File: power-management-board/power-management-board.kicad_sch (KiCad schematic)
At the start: 51 parts, among them IC1 LM74502QDDFRQ1, IC2 TLP7820_TP4,E, J1 Conn_01x02, J2 Conn_01x02, J3 Conn_01x03, J4 Conn_01x04, Q1 XPQR8308QB,LXHQ, Q2 XPQR8308QB,LXHQ, U1 TLP293, U2 TLP293, U3 TLP293, U4 TLP293, U5 TLP3546A, U6 CZ3A07, U7 AP7375

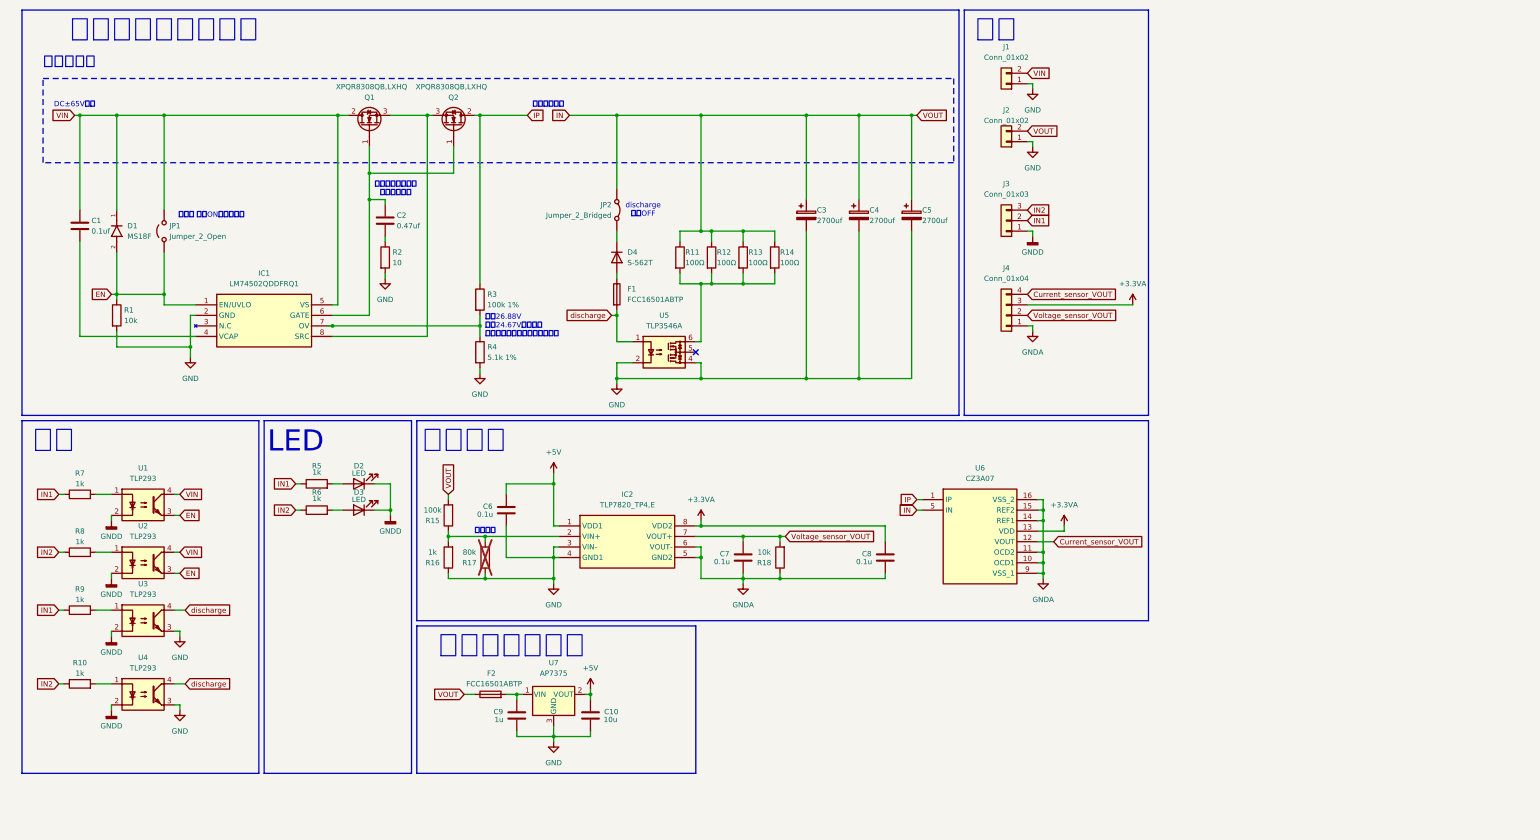
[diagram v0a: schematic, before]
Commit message: 修正版(非常停止はあとで変更します)
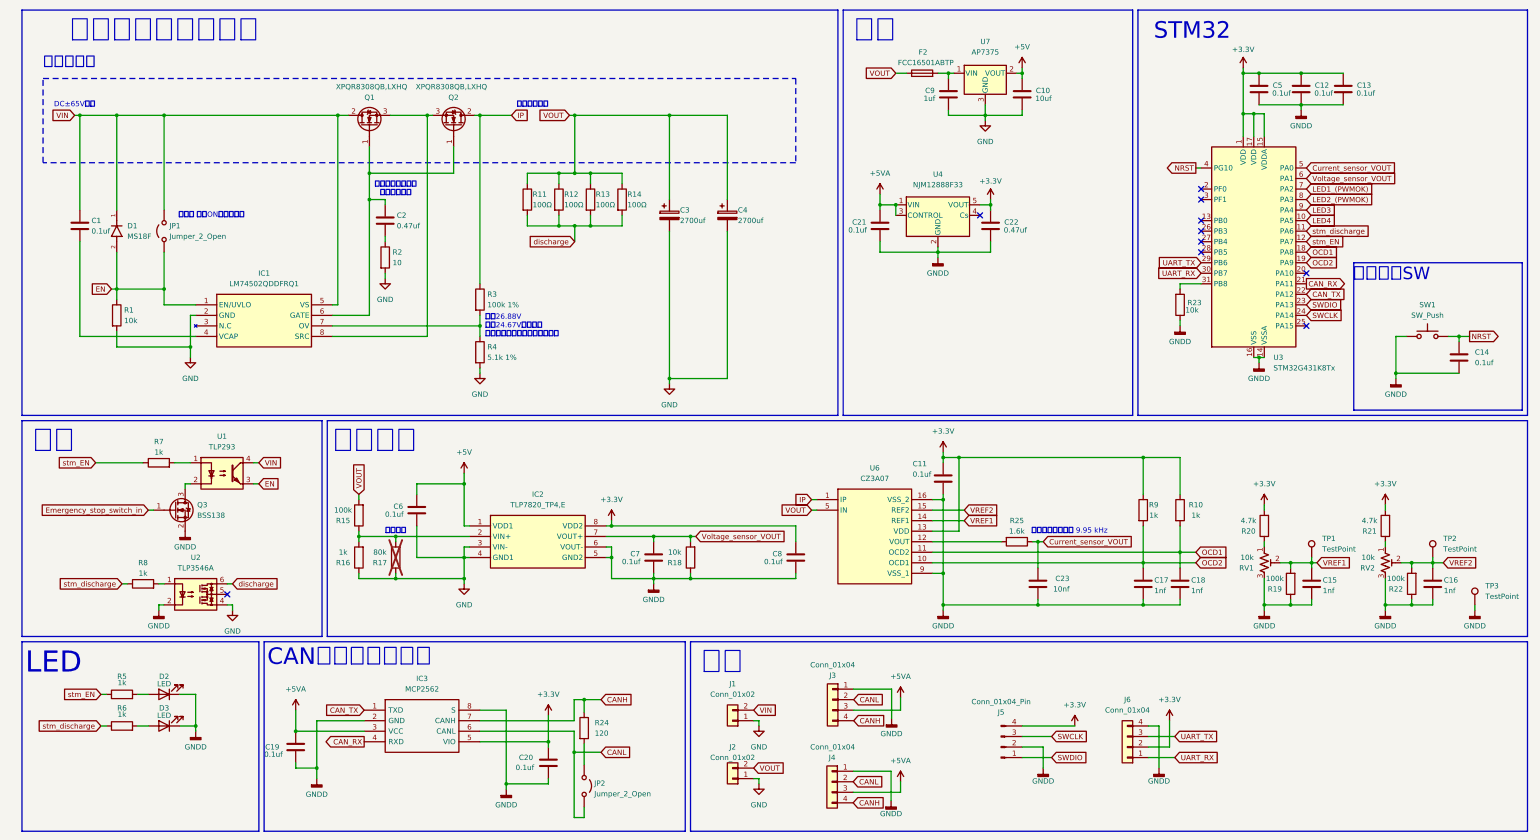
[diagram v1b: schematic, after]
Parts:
- removed C5: 2700uf, Capacitor_THT:CP_Radial_D18.0mm_P7.50mm, symbol Device:C_Polarized
- removed D4: S-562T, 0Ikedalibrary:S-562T, symbol Device:D
- removed F1: FCC16501ABTP, Fuse:Fuse_0603_1608Metric_Pad1.05x0.95mm_HandSolder, symbol Device:Fuse
- removed J3: Conn_01x03, Connector_AMASS:AMASS_MR30PW-M_1x03_P3.50mm_Horizontal, symbol Connector_Generic:Conn_01x03
- removed JP2: Jumper_2_Bridged, Connector_PinHeader_2.54mm:PinHeader_1x02_P2.54mm_Vertical, symbol Jumper:Jumper_2_Bridged
- removed U2, U3, U4: TLP293, Package_SO:SOIC-4_4.55x2.6mm_P1.27mm, symbol Isolator:TLP293
- added C11, C12, C13, C14, C19, C20, C21, C5: 0.1uf, Capacitor_SMD:C_0603_1608Metric_Pad1.08x0.95mm_HandSolder, symbol Device:C
- added C15, C16, C17, C18: 1nf, Capacitor_SMD:C_0603_1608Metric_Pad1.08x0.95mm_HandSolder, symbol Device:C
- added C22: 0.47uf, Capacitor_SMD:C_0603_1608Metric_Pad1.08x0.95mm_HandSolder, symbol Device:C
- added C23: 10nf, Capacitor_SMD:C_0603_1608Metric_Pad1.08x0.95mm_HandSolder, symbol Device:C
- added IC3: MCP2562, 0Ikedalibrary:SOIC127P600X175-8N, symbol 0-Myparts:TJA1441AT_0Z
- added J3, J6: Conn_01x04, Connector_JST:JST_XH_S4B-XH-A_1x04_P2.50mm_Horizontal, symbol Connector_Generic:Conn_01x04
- added J5: Conn_01x04_Pin, Connector_PinHeader_2.54mm:PinHeader_1x04_P2.54mm_Vertical, symbol Connector:Conn_01x04_Pin
- added JP2: Jumper_2_Open, TestPoint:TestPoint_2Pads_Pitch2.54mm_Drill0.8mm, symbol Jumper:Jumper_2_Open
- added Q3: BSS138, Package_TO_SOT_SMD:SOT-23, symbol Transistor_FET:BSS138
- added R19, R22: 100k, Resistor_SMD:R_0603_1608Metric_Pad0.98x0.95mm_HandSolder, symbol Device:R
- added R20, R21: 4.7k, Resistor_SMD:R_0603_1608Metric_Pad0.98x0.95mm_HandSolder, symbol Device:R
- added R23: 10k, Resistor_SMD:R_0603_1608Metric_Pad0.98x0.95mm_HandSolder, symbol Device:R
- added R24: 120, Resistor_SMD:R_0603_1608Metric_Pad0.98x0.95mm_HandSolder, symbol Device:R
- added R25: 1.6k, Resistor_SMD:R_0603_1608Metric_Pad0.98x0.95mm_HandSolder, symbol Device:R
- added RV1, RV2: 10k, Connector_PinHeader_2.54mm:PinHeader_1x03_P2.54mm_Vertical, symbol Device:R_Potentiometer_Trim_US
- added SW1: SW_Push, 0Ikedalibrary:switch_TVAF06-A020B-R, symbol Switch:SW_Push
- added TP1, TP2, TP3: TestPoint, TestPoint:TestPoint_Loop_D1.80mm_Drill1.0mm_Beaded, symbol Connector:TestPoint
- added U3: STM32G431K8Tx, Package_QFP:LQFP-32_7x7mm_P0.8mm, symbol MCU_ST_STM32G4:STM32G431K8Tx
- added U4: NJM12888F33, Package_TO_SOT_SMD:SOT-23-5_HandSoldering, symbol Regulator_Linear:LDK130PU33R_DFN6
- C10: value 10u -> 10uf
- C6, C7, C8: value 0.1u -> 0.1uf
- C9: value 1u -> 1uf
- IC1: footprint SOT65P280X110-8N -> Package_TO_SOT_SMD:SOT-23-8_Handsoldering
- J4: footprint Connector_JST:JST_XH_B4B-XH-A_1x04_P2.50mm_Vertical -> Connector_JST:JST_XH_S4B-XH-A_1x04_P2.50mm_Horizontal
- renumbered U5 to U2
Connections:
- net Current_sensor_VOUT: now also C23.2, R25.1, U3.5 (PA0); no longer J4.4 (Pin_4), U6.12 (VOUT)
- net GND: no longer U2.2
- net GNDD: now also C7.2, C8.2, IC2.5 (GND2), IC2.6 (VOUT-), J4.1 (Pin_1), R18.1, U2.2, U6.16 (VSS_2), U6.9 (VSS_1), C11.2, C12.2, C13.2, C14.2, C15.2, C16.2, C17.2, C18.2, C19.2, C20.2, C21.2, C22.2, C23.1, C5.2, IC3.2 (GND), IC3.8 (S), J3.1 (Pin_1), J5.2 (Pin_2), J6.4 (Pin_4), Q3.2 (S), R19.1, R22.1, R23.1, RV1.3, RV2.3, SW1.1, TP3.1, U3.14 (VSSA), U3.16 (VSS), U3.32 (VSS), U4.2 (GND); no longer U1.2
- net Voltage_sensor_VOUT: now also U3.6 (PA1); no longer J4.2 (Pin_2)
- net discharge: now also R11.2, R12.2, R13.2, R14.2, U2.6; no longer U2.1
- net OCD2: now reaches R9.2
- net OCD2: now also U6.10 (OCD1), C17.1, U3.19 (PA9)
- net at R8.2: now also U2.1
- net OCD1: now reaches R10.2
- net OCD1: now also U6.11 (OCD2), C18.1, U3.18 (PA8)
- net +3.3VA renamed +3.3V
- net +3.3V: now also R10.1, R9.1, C11.1, C12.1, C13.1, C20.1, C22.1, C5.1, IC3.5 (VIO), J5.4 (Pin_4), J6.2 (Pin_2), R20.2, R21.2, U3.1 (VDD), U3.15 (VDDA), U3.17 (VDD), U4.5 (VOUT); no longer J4.3 (Pin_3)
- removed net GNDA: C7.2, C8.2, IC2.5 (GND2), IC2.6 (VOUT-), J4.1 (Pin_1), R18.1, U6.10 (OCD1), U6.11 (OCD2), U6.14 (REF1), U6.15 (REF2), U6.16 (VSS_2), U6.9 (VSS_1)
- net IN renamed VOUT
- net IN1 renamed stm_EN
- net stm_EN: now also U3.12 (PA7); no longer R9.1
- net IN2 renamed stm_discharge
- net stm_discharge: now also U3.11 (PA6); no longer R10.1
- new net: Q3.3 (D), U1.2
- new net: R20.1, RV1.1
- new net: R23.2, U3.31 (PB8)
- new net: R21.1, RV2.1
- new net: JP2.1 (A), R24.2
- new net: R25.2, U6.12 (VOUT)
- new net +5VA: C19.1, C21.1, IC3.3 (VCC), J3.3 (Pin_3), J4.3 (Pin_3), U4.1 (VIN), U4.3 (CONTROL)
- new net CANH: IC3.7 (CANH), J3.4 (Pin_4), J4.4 (Pin_4), R24.1
- new net CANL: IC3.6 (CANL), J3.2 (Pin_2), J4.2 (Pin_2), JP2.2 (B)
- new net CAN_RX: IC3.4 (RXD), U3.21 (PA11)
- new net CAN_TX: IC3.1 (TXD), U3.22 (PA12)
- new net Emergency_stop_switch_in: Q3.1 (G)
- new net LED1_(PWMOK): U3.7 (PA2)
- new net LED2_(PWMOK): U3.8 (PA3)
- new net LED3: U3.9 (PA4)
- new net LED4: U3.10 (PA5)
- new net NRST: C14.1, SW1.2, U3.4 (PG10)
- new net SWCLK: J5.3 (Pin_3), U3.24 (PA14)
- new net SWDIO: J5.1 (Pin_1), U3.23 (PA13)
- new net UART_RX: J6.1 (Pin_1), U3.30 (PB7)
- new net UART_TX: J6.3 (Pin_3), U3.29 (PB6)
- new net VREF1: C15.1, R19.2, RV1.2, TP1.1, U6.14 (REF1)
- new net VREF2: C16.1, R22.2, RV2.2, TP2.1, U6.15 (REF2)
- no-connect marks 1 -> 10
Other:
- note added: "CANトランシーバー"
- note added: "STM32"
- note added: "リセットSW"
- note added: "ローパスフィルタ 9.95 kHz"
- note added: "電源"
- note removed: "discharge 常時OFF"
- note removed: "センサー用電源"
- moved on the sheet: C10, C3, C4, C6, C7, C8, C9, D2, D3, F2, IC2, J1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

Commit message: 修正版完成
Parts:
- removed Q3: BSS138, Package_TO_SOT_SMD:SOT-23, symbol Transistor_FET:BSS138
- added D4, D8: SS2040FL, 0Ikedalibrary:SOD-123FL, symbol Device:D
- added D5, D6, D7: LED, LED_SMD:LED_0603_1608Metric_Pad1.05x0.95mm_HandSolder, symbol Device:LED
- added J7, J8: Conn_01x02, 0Ikedalibrary:AMASS_XT60-F_1x02_P7.20mm_Vertical, symbol Connector_Generic:Conn_01x02
- added R26: 10k, Resistor_SMD:R_0603_1608Metric_Pad0.98x0.95mm_HandSolder, symbol Device:R
- added R27, R28, R29: 1k, Resistor_SMD:R_0603_1608Metric_Pad0.98x0.95mm_HandSolder, symbol Device:R
- added R30: 100, Resistor_SMD:R_0603_1608Metric_Pad0.98x0.95mm_HandSolder, symbol Device:R
- added U5: TLP293, Package_SO:SOIC-4_4.55x2.6mm_P1.27mm, symbol Isolator:TLP293
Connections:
- net +3.3V: now also R29.1
- net Emergency_stop_switch_in: now also R7.1, J8.2 (Pin_2), R27.1, R28.1
- net GNDD: now also D8.2 (A), J7.1 (Pin_1), R26.2, U5.3
- net stm_EN: no longer R7.1, U3.12 (PA7)
- net GNDA: now reaches U1.2
- net GNDA: now also D5.2 (A), D6.1 (K), D7.2 (A), J8.1 (Pin_1), U5.2
- net at R7.2, U1.1: now also D5.1 (K)
- net EN_return: now reaches U3.20 (PA10)
- net EN_return: now also R29.2, U5.4
- new net: D7.1 (K), R28.2, U5.1
- new net: J7.2 (Pin_2), R30.1
- new net: D6.2 (A), R27.2
- new net Emergency_stop_switch_out: D4.1 (K), D8.1 (K), R30.2
- new net stm32_EN: D4.2 (A), R26.1, U3.12 (PA7)
- no-connect marks 10 -> 9
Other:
- moved on the sheet: C11, C14, C15, C16, C17, C18, C19, C20, C23, C6, C7, C8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

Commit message: 仮配置完了
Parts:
- removed D5, D7: LED, LED_SMD:LED_0603_1608Metric_Pad1.05x0.95mm_HandSolder, symbol Device:LED
- removed J6: Conn_01x04, Connector_JST:JST_XH_S4B-XH-A_1x04_P2.50mm_Horizontal, symbol Connector_Generic:Conn_01x04
- added D10, D5, D7, D9: SS2040FL, 0Ikedalibrary:SOD-123FL, symbol Device:D
- added D11, D12, D13, D14, D15, D16, D17, D18: LED, LED_SMD:LED_0603_1608Metric_Pad1.05x0.95mm_HandSolder, symbol Device:LED
- added J6: Conn_01x02_Pin, TestPoint:TestPoint_2Pads_Pitch2.54mm_Drill0.8mm, symbol Connector:Conn_01x02_Pin
- added J9: Conn_01x03, Connector_AMASS:AMASS_MR30PW-M_1x03_P3.50mm_Horizontal, symbol Connector_Generic:Conn_01x03
- added R31, R32, R33, R34, R35, R36, R37, R38, R39, R40, R41: 1k, Resistor_SMD:R_0603_1608Metric_Pad0.98x0.95mm_HandSolder, symbol Device:R
- added SW2: SW_SPDT_312, 0Ikedalibrary:CJS1200A1, symbol Switch:SW_SPDT_312
- added U8, U9: TLP293, Package_SO:SOIC-4_4.55x2.6mm_P1.27mm, symbol Isolator:TLP293
- J3, J4: footprint Connector_JST:JST_XH_S4B-XH-A_1x04_P2.50mm_Horizontal -> Connector_JST:JST_XH_B4B-XH-A_1x04_P2.50mm_Vertical
- J7: footprint 0Ikedalibrary:AMASS_XT60-F_1x02_P7.20mm_Vertical -> Connector_AMASS:AMASS_XT60-M_1x02_P7.20mm_Vertical
- JP2: footprint TestPoint:TestPoint_2Pads_Pitch2.54mm_Drill0.8mm -> Connector_PinHeader_2.54mm:PinHeader_1x02_P2.54mm_Vertical
- RV1, RV2: footprint Connector_PinHeader_2.54mm:PinHeader_1x03_P2.54mm_Vertical -> Potentiometer_THT:Potentiometer_Bourns_3296W_Vertical
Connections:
- net stm_EN is gone; now on net stm32_EN: R5.1
- net +3.3V: now also R32.1, R34.1
- net GND: now also U2.6, D11.1 (K), D12.2 (A), SW2.2 (B); no longer U2.4
- net GNDA: now also D5.2 (A), D7.2 (A)
- net GNDD: now also D13.1 (K), D14.1 (K), D15.1 (K), D16.1 (K), U8.3, U9.3
- net LED1_(PWMOK): now also R36.1
- net LED2_(PWMOK): now also R37.1
- net LED3: now also R38.1
- net LED4: now also R39.1
- net UART_RX: now also J6.2 (Pin_2)
- net UART_TX: now also J6.1 (Pin_1)
- net VIN: now also R35.1
- net discharge: now also U2.4; no longer U2.6
- net stm32_EN: now also U3.27 (PB4); no longer U3.12 (PA7)
- net stm_discharge: now also U3.26 (PB3); no longer U3.11 (PA6)
- net at R7.2, U1.1: now also D7.1 (K)
- net at IC1.7 (OV), R3.2, R4.1: now also SW2.3 (C)
- net at R28.2, U5.1: now also D5.1 (K)
- new net: D10.1 (K), R33.2, U9.1
- new net: D9.1 (K), R31.2, U8.1
- new net: D13.2 (A), R36.2
- new net: D11.2 (A), D12.1 (K), R35.2
- new net: D17.2 (A), R40.2
- new net: D18.2 (A), R41.2
- new net: D16.2 (A), R39.2
- new net: D14.2 (A), R37.2
- new net: D15.2 (A), R38.2
- new net GND1: D10.2 (A), D17.1 (K), D18.1 (K), D9.2 (A), J9.1 (Pin_1), U8.2, U9.2
- new net IN1: J9.2 (Pin_2), R31.1, R40.1
- new net IN2: J9.3 (Pin_3), R33.1, R41.1
- new net stm32_IN1: R32.2, U3.12 (PA7), U8.4
- new net stm32_IN2: R34.2, U3.11 (PA6), U9.4
- no-connect marks 9 -> 8
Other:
- moved on the sheet: C11, C12, C13, C15, C16, C17, C18, C19, C20, C23, C5, C6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

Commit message: 完成(ビア以外)
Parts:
- removed JP2: Jumper_2_Open, Connector_PinHeader_2.54mm:PinHeader_1x02_P2.54mm_Vertical, symbol Jumper:Jumper_2_Open
- added D19, D20, D21, D22: LED, LED_SMD:LED_0603_1608Metric_Pad1.05x0.95mm_HandSolder, symbol Device:LED
- added R42, R43, R44, R45: 1k, Resistor_SMD:R_0603_1608Metric_Pad0.98x0.95mm_HandSolder, symbol Device:R
- added SW3: SW_SPDT_312, 0Ikedalibrary:CJS1200A1, symbol Switch:SW_SPDT_312
- J3, J4: footprint Connector_JST:JST_XH_B4B-XH-A_1x04_P2.50mm_Vertical -> Connector_JST:JST_XH_S4B-XH-A_1x04_P2.50mm_Horizontal
- U6: footprint CZ3A07 -> 0Ikedalibrary:CZ3A07
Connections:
- net +3.3V: now also R43.1
- net +5V: now also R45.1
- net +5VA: now also R42.1
- net CANL: now also SW3.2 (B)
- net GND: now also U2.4, D21.1 (K), D22.1 (K); no longer U2.6
- net GNDD: now also D19.1 (K), D20.1 (K)
- net VOUT: now also R44.1
- net discharge: now also U2.6; no longer U2.4
- net at R24.2: now also SW3.1 (A)
- new net: D21.2 (A), R44.2
- new net: D20.2 (A), R43.2
- new net: D19.2 (A), R42.2
- new net: D22.2 (A), R45.2
- no-connect marks 8 -> 9
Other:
- moved on the sheet: C19, C20, D11, D12, D13, D14, D15, D16, D17, D18, D2, D3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
